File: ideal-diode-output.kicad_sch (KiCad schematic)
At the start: 1 part, among them U3 LM5050-1

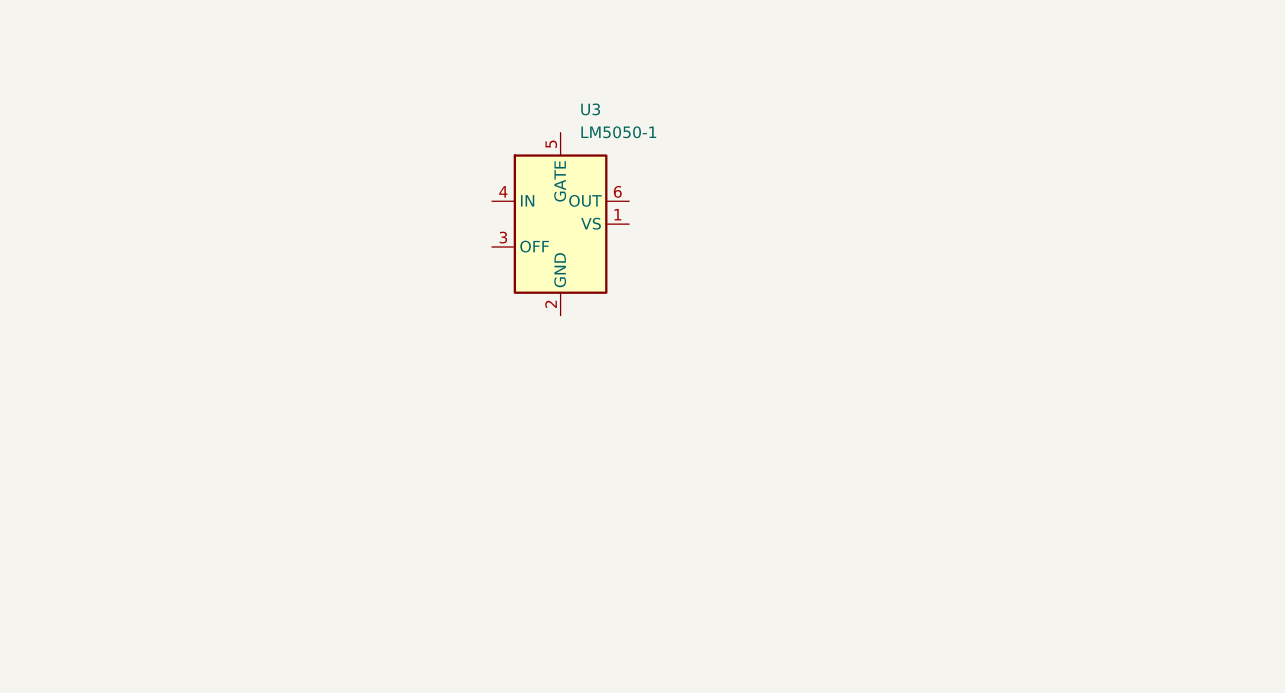
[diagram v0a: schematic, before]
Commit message: added ideal diode
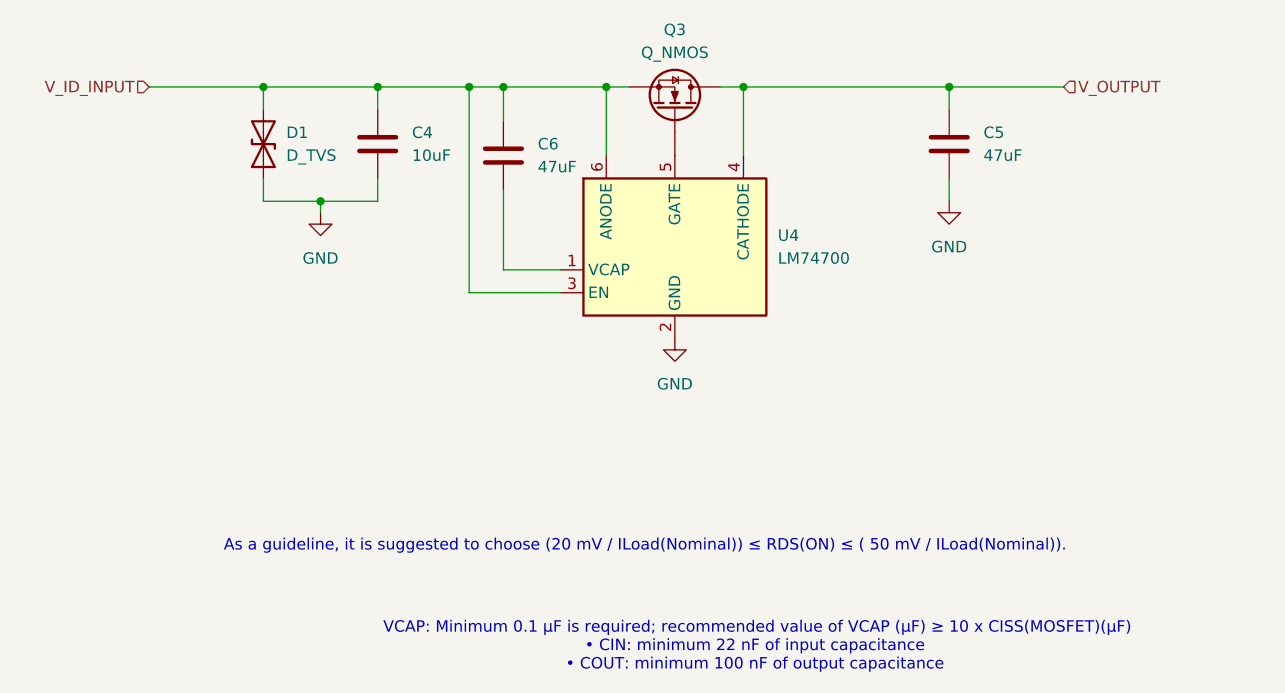
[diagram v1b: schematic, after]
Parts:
- removed U3: LM5050-1, Package_TO_SOT_SMD:TSOT-23-6_HandSoldering, symbol Power_Management:LM5050-1
- added C4: 10uF, symbol Device:C
- added C5, C6: 47uF, symbol Device:C
- added D1: D_TVS, symbol Device:D_TVS
- added Q3: Q_NMOS, symbol Device:Q_NMOS
- added U4: LM74700, Package_TO_SOT_SMD:SOT-23-6, symbol Power_Management:LM74700
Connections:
- new net: Q3.G, U4.5 (GATE)
- new net: C6.2, U4.1 (VCAP)
- new net GND: C4.2, C5.2, D1.1 (A1), U4.2 (GND)
- new net V_ID_INPUT: C4.1, C6.1, D1.2 (A2), Q3.S, U4.3 (EN), U4.6 (ANODE)
- new net V_OUTPUT: C5.1, Q3.D, U4.4 (CATHODE)
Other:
- note added: "As a guideline, it is suggested to choose (20 mV / ILoad(Nominal)) ≤ RDS(ON) ≤ ( 50 mV / ILoad(Nominal))."
- note added: "VCAP: Minimum 0.1 µF is required; recommended value of VCAP (µF) ≥ 10 x CISS(MOSFET)(µF) • CIN: minimum 22 nF of input capacitance • COUT: minimum 100 nF of output capacitance"
